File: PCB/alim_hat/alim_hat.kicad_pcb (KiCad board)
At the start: 4 copper layers, 85 x 56 mm, 49 parts, among them J1 Screw_Terminal_01x04, J10 Conn_01x02, J11 Conn_01x02, J12 Conn_01x02, J13 Conn_01x02, J14 Conn_01x02, J15 Conn_01x02, J16 Conn_01x02, J17 Conn_01x02, J2 Conn_01x02_Male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

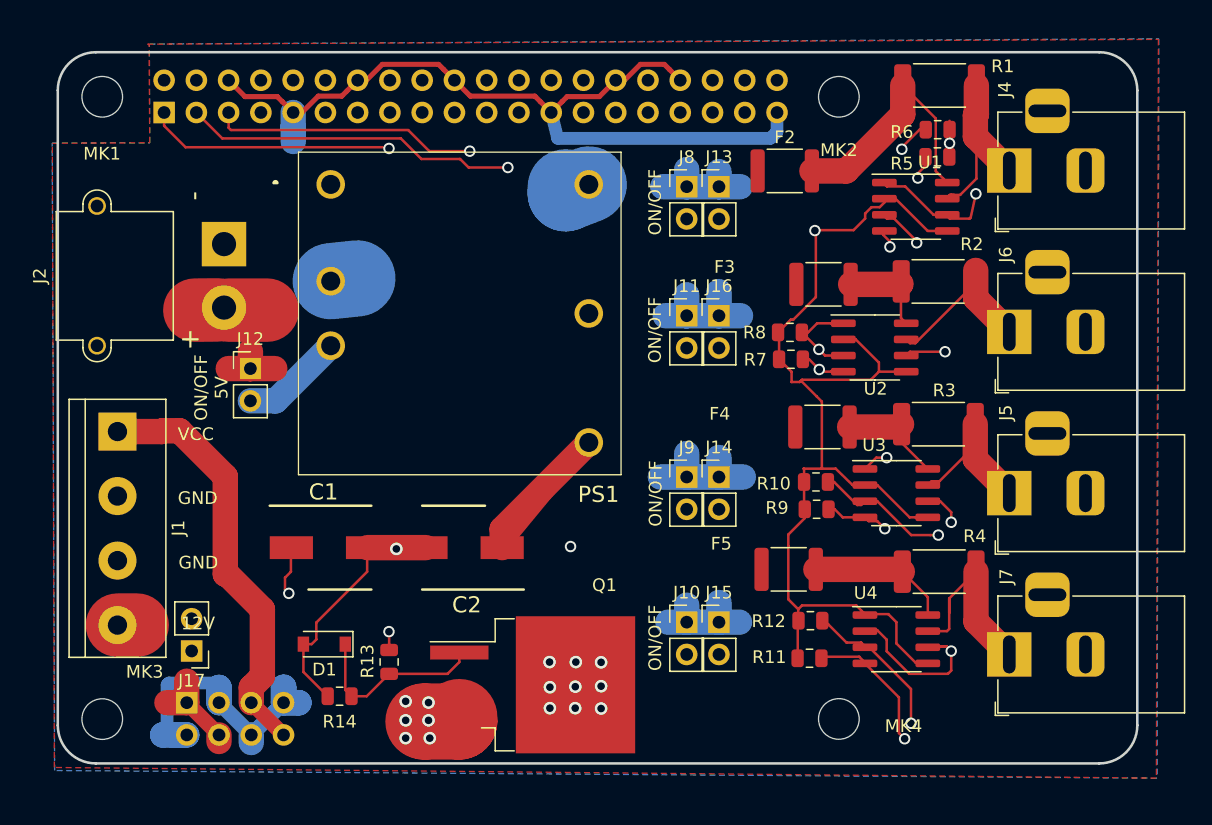
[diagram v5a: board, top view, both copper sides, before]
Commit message: change trace for CP capa
help jlcpcb analyse
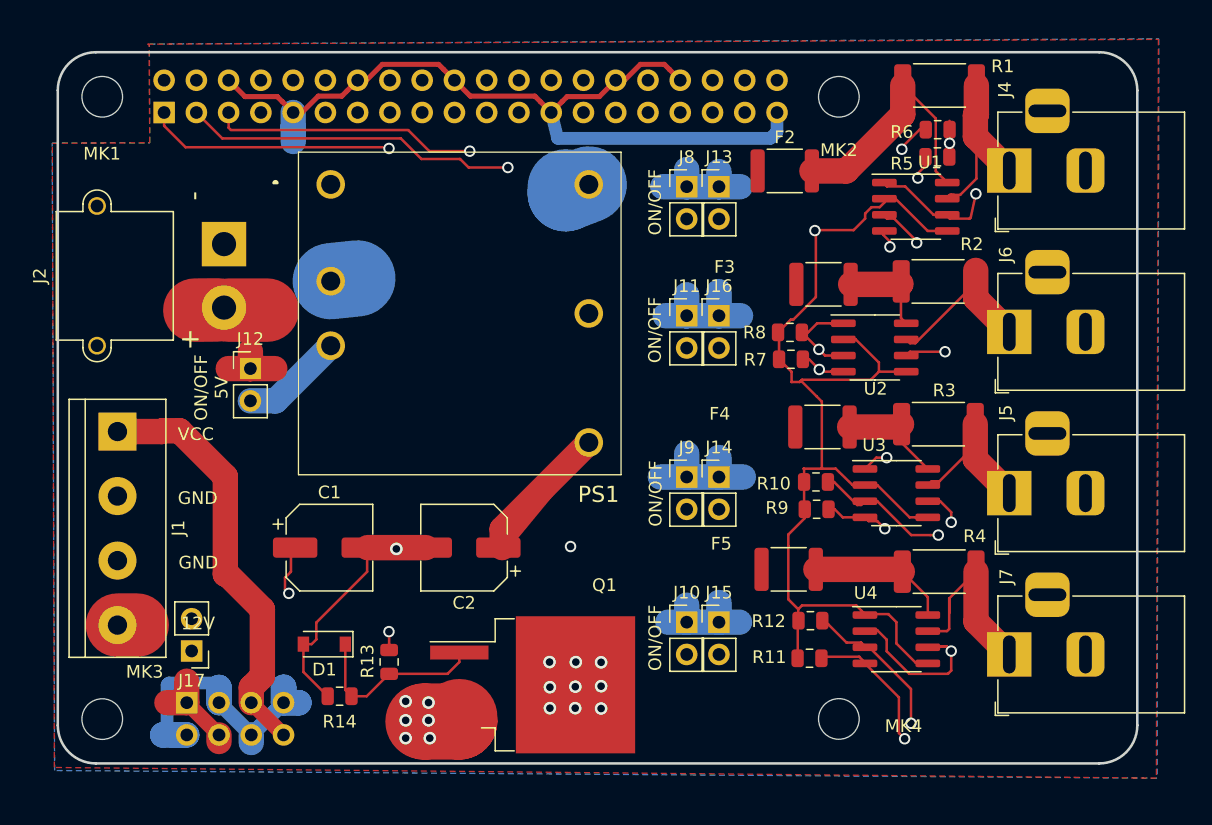
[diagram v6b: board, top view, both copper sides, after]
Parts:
- C1, C2: footprint capa:CAPAE660X800N -> Capacitor_SMD:CP_Elec_6.3x7.7
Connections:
- P1 pad 10: (no net) -> /UART_RX
- P1 pad 11: (no net) -> /GPIO17
- P1 pad 12: (no net) -> /GPIO18
- P1 pad 13: (no net) -> /GPIO27
- P1 pad 15: (no net) -> /GPIO22
- P1 pad 16: (no net) -> /GPIO23
- P1 pad 18: (no net) -> /GPIO24
- P1 pad 19: (no net) -> Net-(P1-Pad19)
- P1 pad 21: (no net) -> Net-(P1-Pad21)
- P1 pad 22: (no net) -> /GPIO25
- P1 pad 23: (no net) -> Net-(P1-Pad23)
- P1 pad 24: (no net) -> Net-(P1-Pad24)
- P1 pad 26: (no net) -> Net-(P1-Pad26)
- P1 pad 27: (no net) -> Net-(P1-Pad27)
- P1 pad 28: (no net) -> Net-(P1-Pad28)
- P1 pad 29: (no net) -> /GPIO5
- P1 pad 31: (no net) -> /GPIO6
- P1 pad 32: (no net) -> /GPIO12(PWM0)
- P1 pad 33: (no net) -> /GPIO13(PWM1)
- P1 pad 35: (no net) -> Net-(P1-Pad35)
- P1 pad 36: (no net) -> /GPIO16
- P1 pad 37: (no net) -> /GPIO26
- P1 pad 38: (no net) -> Net-(P1-Pad38)
- P1 pad 40: (no net) -> Net-(P1-Pad40)
- P1 pad 7: (no net) -> /1-wire
- P1 pad 8: (no net) -> /UART_TX
- PS1 pad 1: (no net) -> Net-(PS1-Pad1)
- PS1 pad 5: (no net) -> Net-(PS1-Pad5)

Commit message: upgrade relais hat and all hat to kicad 7.0
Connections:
- net +3V3 renamed +3.3V
- P1 pad 19: Net-(P1-Pad19) -> unconnected-(P1-Pin_19-Pad19)
- P1 pad 21: Net-(P1-Pad21) -> unconnected-(P1-Pin_21-Pad21)
- P1 pad 23: Net-(P1-Pad23) -> unconnected-(P1-Pin_23-Pad23)
- P1 pad 24: Net-(P1-Pad24) -> unconnected-(P1-Pin_24-Pad24)
- P1 pad 26: Net-(P1-Pad26) -> unconnected-(P1-Pin_26-Pad26)
- P1 pad 27: Net-(P1-Pad27) -> unconnected-(P1-Pin_27-Pad27)
- P1 pad 28: Net-(P1-Pad28) -> unconnected-(P1-Pin_28-Pad28)
- P1 pad 35: Net-(P1-Pad35) -> unconnected-(P1-Pin_35-Pad35)
- P1 pad 38: Net-(P1-Pad38) -> unconnected-(P1-Pin_38-Pad38)
- P1 pad 40: Net-(P1-Pad40) -> unconnected-(P1-Pin_40-Pad40)
- PS1 pad 1: Net-(PS1-Pad1) -> unconnected-(PS1-CTRL-Pad1)
- PS1 pad 5: Net-(PS1-Pad5) -> unconnected-(PS1-TRIM-Pad5)
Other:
- net class Default removed
- net class Power removed
